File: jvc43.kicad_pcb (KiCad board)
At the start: 6 copper layers, 101.6 x 50.8 mm, 119 parts, among them J201 8P8C_LED_Shielded, J301 8P8C_LED_Shielded, J401 USB_C_Receptacle_USB2.0, U201 LAN8810, U301 LAN8810, U401 LTC3622*DE

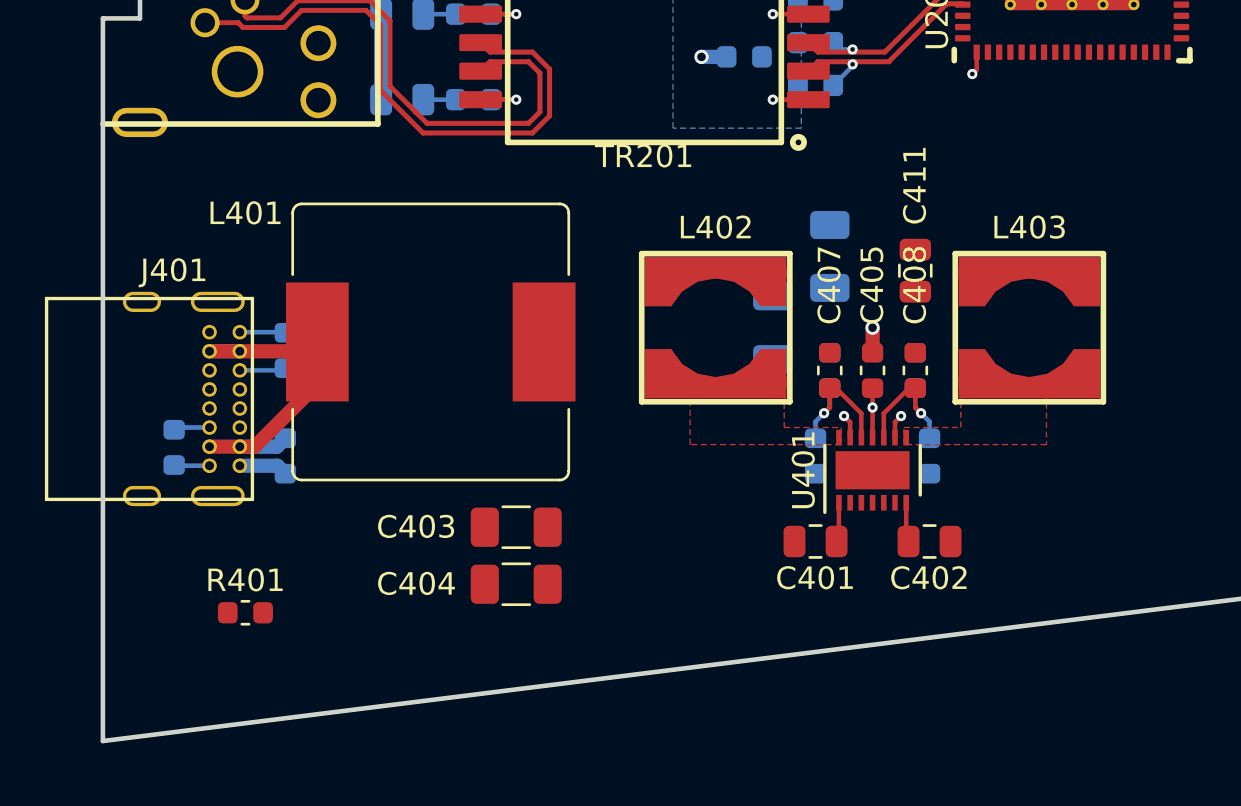
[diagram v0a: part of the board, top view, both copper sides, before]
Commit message: Major work on the power supply: - Swapped the input filter inductor for a significantly smaller one - Basically finished laying out the switching supply
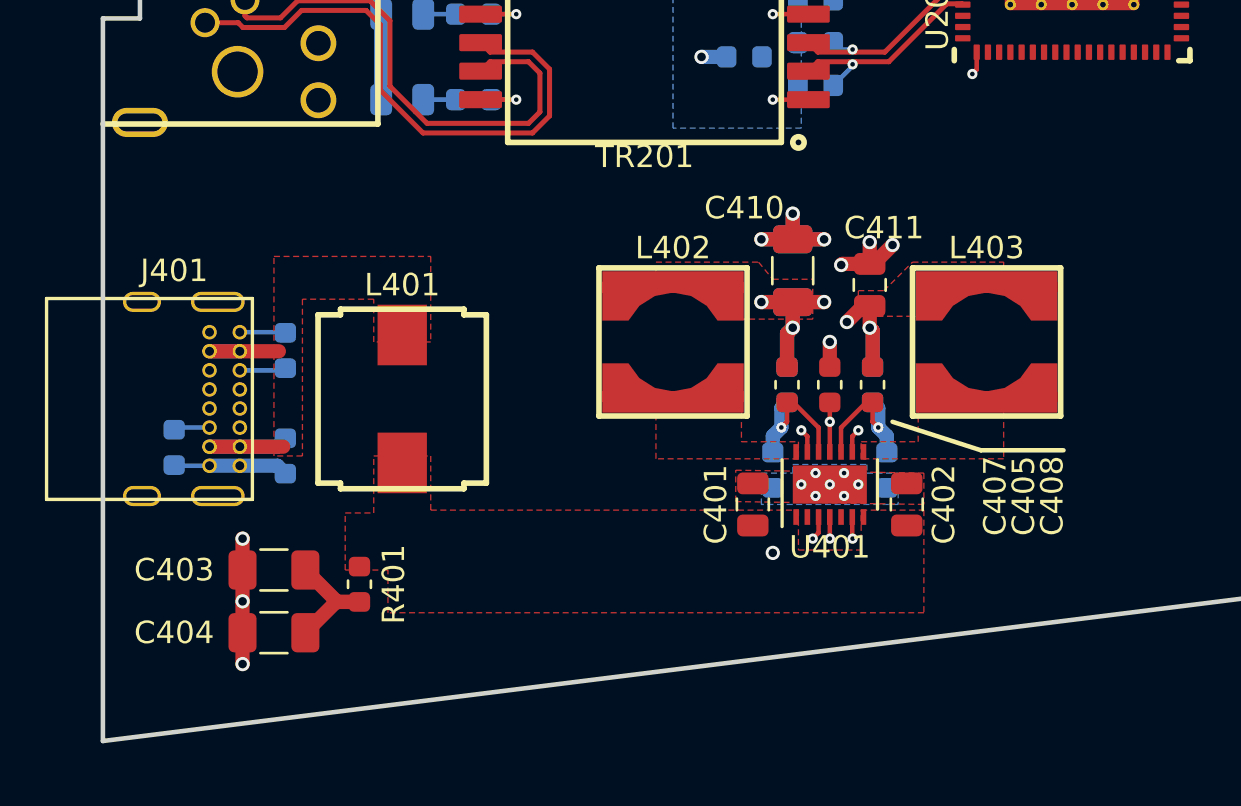
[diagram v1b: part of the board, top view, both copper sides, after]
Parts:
- C410: moved to F.Cu
- L401: footprint Inductor_SMD:L_Bourns_SRR1210A -> myfp:L_Panasonic_ETQ-P4MxxxKFM
- moved C404 11.0 mm to (33.0, 71.4), turned to 180 degrees
- moved C403 11.0 mm to (33.0, 68.6), turned to 180 degrees
- moved R401 5.24 mm to (36.8, 69.2), turned to 270 degrees
- moved C401 3.25 mm to (54.4, 65.7), turned to 90 degrees
- moved L401 2.84 mm to (38.7, 61.0), turned to 270 degrees
- moved C409 2.69 mm to (56.1, 55.2), turned to 90 degrees
- moved C411 2.13 mm to (59.6, 55.9)
- moved C405 2.01 mm to (57.8, 60.3)
- moved C408 2.01 mm to (59.7, 60.3)
- moved L402 2.01 mm to (50.8, 58.4)
- moved L403 2.01 mm to (64.8, 58.4)
- moved R405 2.01 mm to (59.7, 60.3)
- moved R406 2.01 mm to (55.2, 64.1)
- moved U401 2.01 mm to (57.8, 64.8)
- moved C407 2.01 mm to (55.9, 60.3)
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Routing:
- net GND: track 28.7 -> 49.2 mm, vias 14 -> 32
- net +1V2: track 0.00 -> 11.6 mm, vias 0 -> 3
- net /Power_Supply/IntVcc: track 2.21 -> 10.9 mm, vias 1 -> 2
- net /Power_Supply/Vin_damp: track 0.00 -> 5.98 mm
- net +2V5: track 0.00 -> 5.89 mm, vias 0 -> 2
- net /Power_Supply/VCC_USB: track 16.3 -> 11.3 mm
- net /Power_Supply/PS_Vin: track 5.68 -> 2.91 mm, vias 2 -> 3
- added copper zone on F.Cu, net +1V2
- added copper zone on F.Cu, net +2V5
- added copper zone on F.Cu, net /Power_Supply/PS_Vin
- added copper zone on L3.Cu, net /Power_Supply/PS_Vin
- added copper zone on F.Cu, net /Power_Supply/VCC_USB
- added copper zone on B.Cu, net GND
- added copper zone on F.Cu, net GND

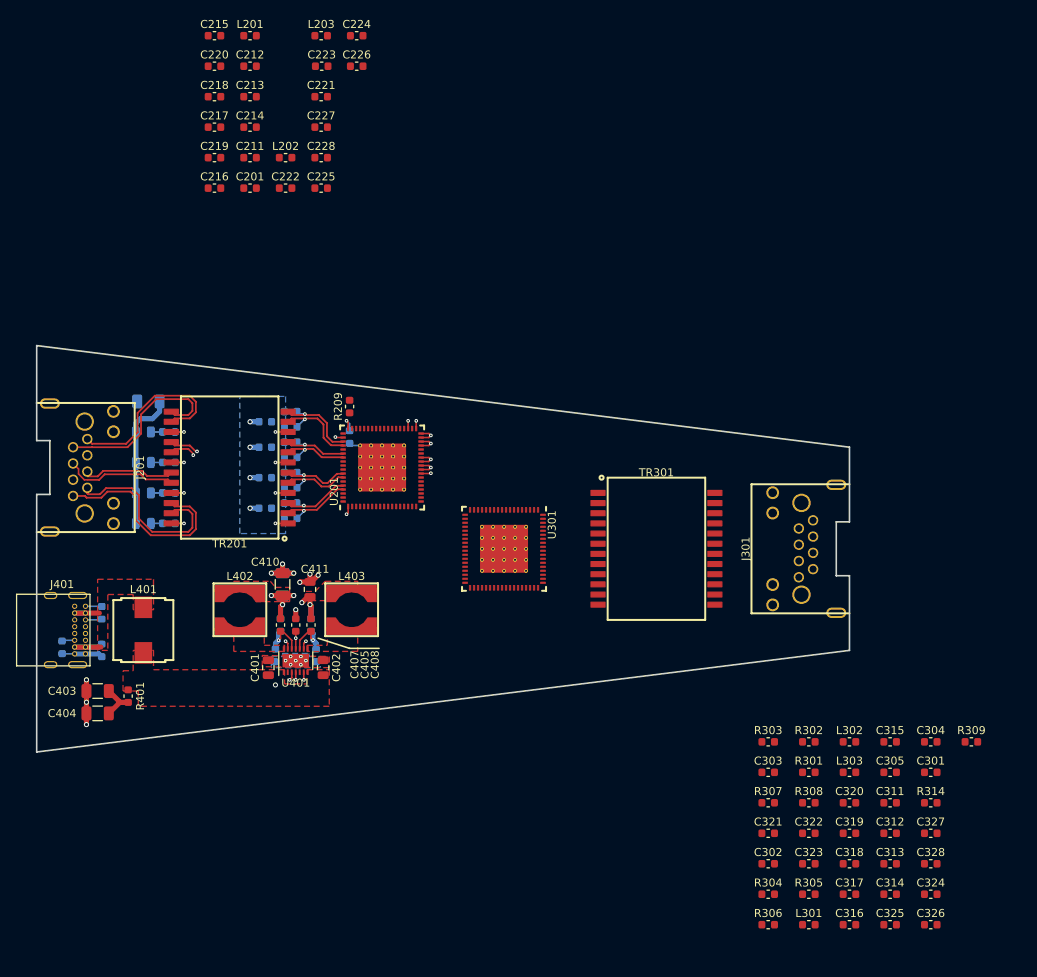
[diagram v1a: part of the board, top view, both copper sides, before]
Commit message: Forward progress - Started the real 1.2V power plane - Placed and routed most of PHY1 decoupling capacitors - Placed and partly routed transformer2 PHY-side resistors & capacitors - Labelled a few more nets for clarity during layout
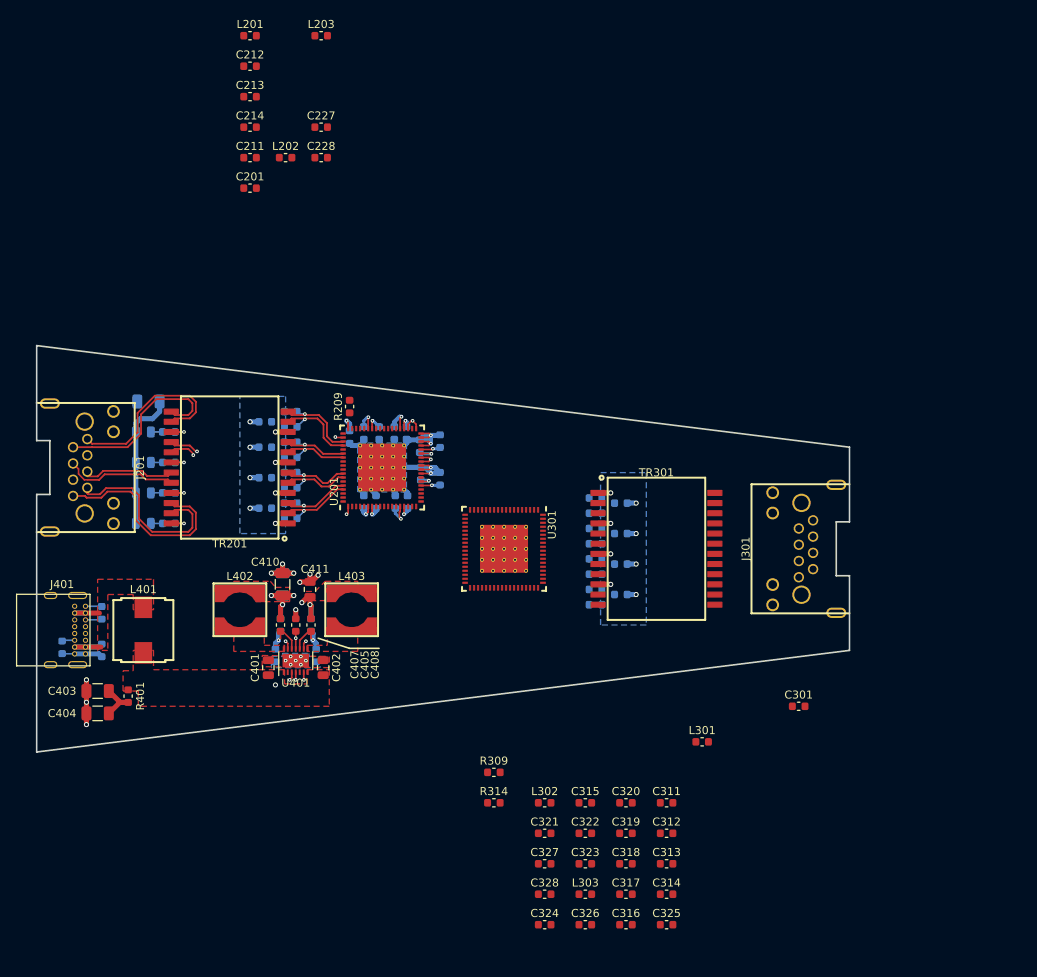
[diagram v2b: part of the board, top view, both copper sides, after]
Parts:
- C215, C216, C217, C218, C219, C220, C221, C222, C223, C224, C225, C226, C302, C303, C304, C305, R301, R302, R303, R304, R305, R306, R307, R308: moved to B.Cu
- moved C215 61.2 mm to (66.3, 45.0), turned to 90 degrees
- moved R309 59.8 mm to (82.5, 78.7)
- moved R314 54.6 mm to (82.5, 82.5)
- moved R306 54.0 mm to (95.2, 48.3), turned to 180 degrees
- moved C223 52.4 mm to (73.4, 41.4), turned to 90 degrees
- moved C217 52.2 mm to (75.8, 42.0), turned to 90 degrees
- moved C224 51.9 mm to (73.3, 38.0), turned to 90 degrees
- moved C218 51.5 mm to (75.8, 37.3), turned to 90 degrees
- moved R305 51.3 mm to (95.2, 50.2), turned to 180 degrees
- moved C221 51.1 mm to (67.8, 45.0), turned to 90 degrees
- moved C220 49.5 mm to (66.3, 36.3), turned to 270 degrees
- moved C324 48.4 mm to (88.9, 97.8)
- moved C327 48.4 mm to (88.9, 90.2)
- moved C328 48.4 mm to (88.9, 94.0)
- moved C305 47.6 mm to (98.4, 45.1)
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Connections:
- net Net-(U201-Pad20) renamed /Ethernet1/CRS
- net Net-(U201-Pad21) renamed /Ethernet1/COL
- net Net-(U201-Pad3) renamed /Ethernet1/TDO
- net Net-(U201-Pad42) renamed /Ethernet1/ACT_LED
- net Net-(U201-Pad43) renamed /Ethernet1/1000_LED
- net Net-(U201-Pad44) renamed /Ethernet1/100_LED
- net Net-(U201-Pad45) renamed /Ethernet1/10_LED
- net Net-(U201-Pad46) renamed /Ethernet1/CONFIG3
- net Net-(U201-Pad47) renamed /Ethernet1/CONFIG2
- net Net-(U201-Pad5) renamed /Ethernet1/XO
- net Net-(U201-Pad50) renamed /Ethernet1/CONFIG1
- net Net-(U201-Pad51) renamed /Ethernet1/CONFIG0
- net Net-(U201-Pad55) renamed /Ethernet1/nRST
- net Net-(U301-Pad20) renamed /Ethernet2/CRS
- net Net-(U301-Pad21) renamed /Ethernet2/COL
- net Net-(U301-Pad3) renamed /Ethernet2/TDO
- net Net-(U301-Pad42) renamed /Ethernet2/ACT_LED
- net Net-(U301-Pad43) renamed /Ethernet2/1000_LED
- net Net-(U301-Pad44) renamed /Ethernet2/100_LED
- net Net-(U301-Pad45) renamed /Ethernet2/10_LED
- net Net-(U301-Pad46) renamed /Ethernet2/CONFIG3
- net Net-(U301-Pad47) renamed /Ethernet2/CONFIG2
- net Net-(U301-Pad5) renamed /Ethernet2/XO
- net Net-(U301-Pad50) renamed /Ethernet2/CONFIG1
- net Net-(U301-Pad51) renamed /Ethernet2/CONFIG0
- net Net-(U301-Pad55) renamed /Ethernet2/nRST
- C215 pad 1: /Ethernet1/VDDVARIO -> +2V5
- C216 pad 1: /Ethernet1/VDDVARIO -> +2V5
- C217 pad 1: /Ethernet1/VDDVARIO -> +2V5
- C218 pad 1: /Ethernet1/VDDVARIO -> +2V5
- C219 pad 1: /Ethernet1/VDDVARIO -> +2V5
- C220 pad 1: /Ethernet1/VDDVARIO -> +2V5
- C315 pad 1: /Ethernet2/VDDVARIO -> +2V5
- C316 pad 1: /Ethernet2/VDDVARIO -> +2V5
- C317 pad 1: /Ethernet2/VDDVARIO -> +2V5
- C318 pad 1: /Ethernet2/VDDVARIO -> +2V5
- C319 pad 1: /Ethernet2/VDDVARIO -> +2V5
- C320 pad 1: /Ethernet2/VDDVARIO -> +2V5
- L201 pad 1: /Ethernet1/VDDVARIO -> +2V5
- L301 pad 1: /Ethernet2/VDDVARIO -> +2V5
- R209 pad 2: /Ethernet1/VDDVARIO -> +2V5
- R309 pad 2: /Ethernet2/VDDVARIO -> +2V5
- U201 pad 14: /Ethernet1/VDDVARIO -> +2V5
- U201 pad 2: /Ethernet1/VDDVARIO -> +2V5
- U201 pad 23: /Ethernet1/VDDVARIO -> +2V5
- U201 pad 32: /Ethernet1/VDDVARIO -> +2V5
- U201 pad 41: /Ethernet1/VDDVARIO -> +2V5
- U201 pad 49: /Ethernet1/VDDVARIO -> +2V5
- U201 pad 6: /Ethernet1/VDDVARIO -> +2V5
- U201 pad 72: /Ethernet1/VDDVARIO -> +2V5
- U301 pad 14: /Ethernet2/VDDVARIO -> +2V5
- U301 pad 2: /Ethernet2/VDDVARIO -> +2V5
- U301 pad 23: /Ethernet2/VDDVARIO -> +2V5
- U301 pad 32: /Ethernet2/VDDVARIO -> +2V5
- U301 pad 4: /Ethernet2/XI -> /Ethernet1/XI
- U301 pad 41: /Ethernet2/VDDVARIO -> +2V5
- U301 pad 49: /Ethernet2/VDDVARIO -> +2V5
- U301 pad 6: /Ethernet2/VDDVARIO -> +2V5
- U301 pad 72: /Ethernet2/VDDVARIO -> +2V5
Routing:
- net GND: track 49.2 -> 76.8 mm, vias 32 -> 35
- net +2V5: track 5.89 -> 22.2 mm, vias 2 -> 8
- net +1V2: track 11.6 -> 24.2 mm, vias 3 -> 9
- net /Ethernet2/VDD_ETH: track 0.00 -> 6.35 mm, vias 0 -> 4
- added copper zone on L3.Cu, net +1V2
- added copper zone on L5.Cu, net +2V5
- added copper zone on B.Cu, net /Ethernet2/VDD_ETH
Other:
- net class CloseSig added: clearance 0.1778, trace_width 0.2032, via_dia 0.4572, via_drill 0.2032

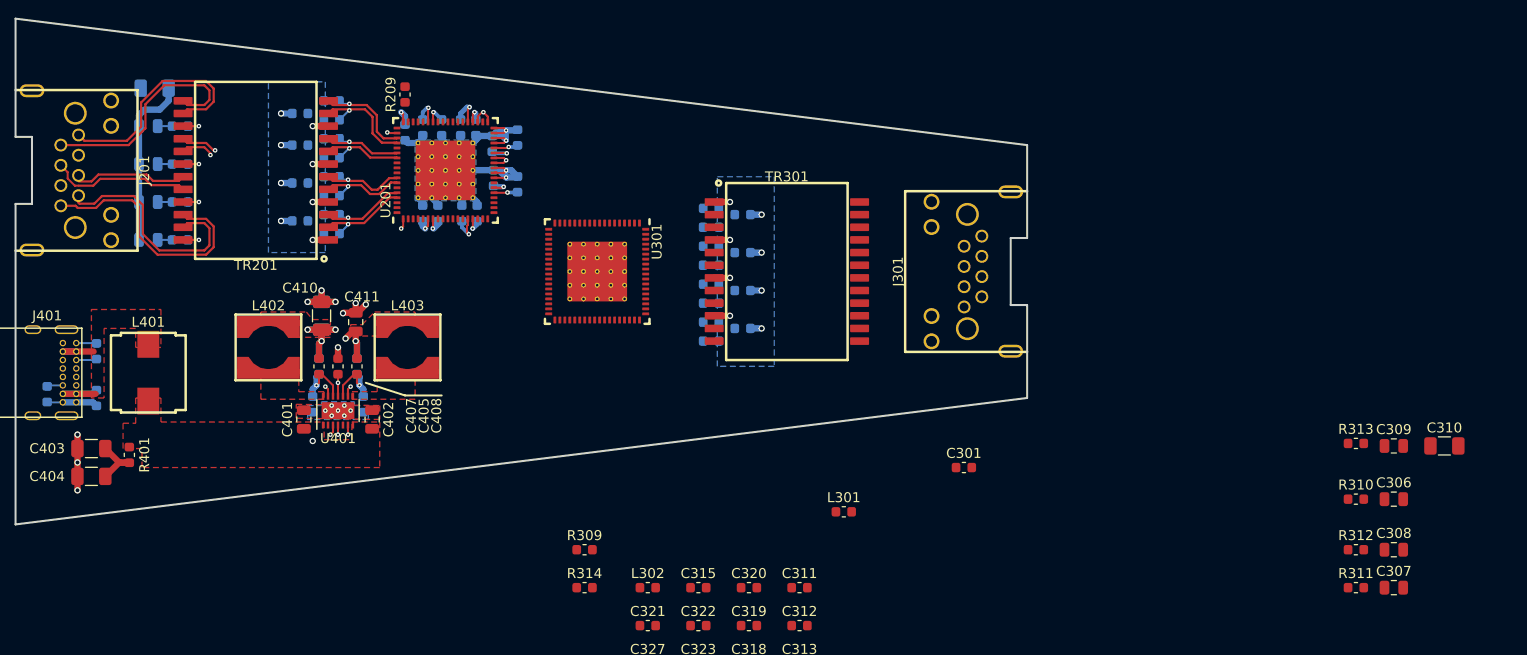
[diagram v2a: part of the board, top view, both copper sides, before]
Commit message: Routed Ethernet2 RJ45-to-transformer area.
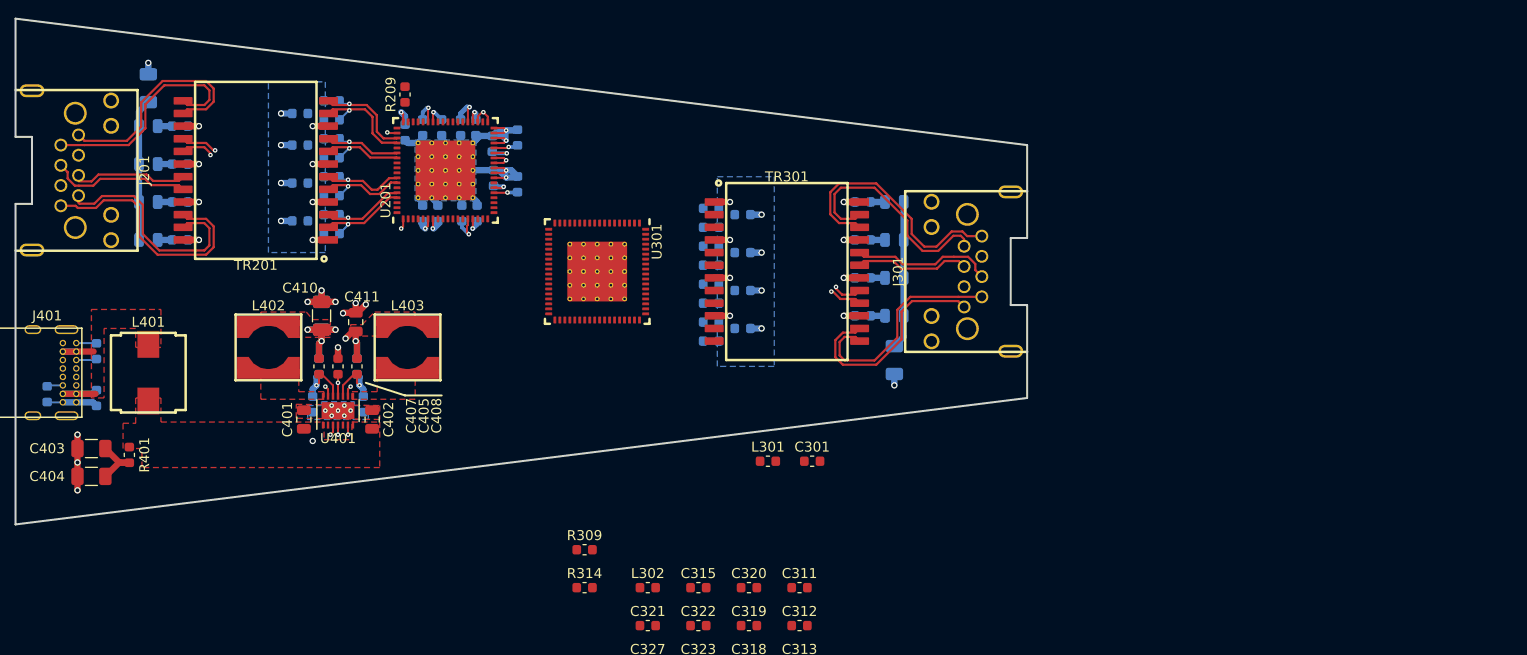
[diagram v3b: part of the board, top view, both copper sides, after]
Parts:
- C306, C307, C308, C309, C310, R310, R311, R312, R313: moved to B.Cu
- moved C307 59.0 mm to (113.7, 51.4)
- moved C308 59.0 mm to (113.7, 47.6)
- moved R311 58.5 mm to (110.5, 51.4)
- moved R312 58.5 mm to (110.5, 47.6)
- moved C310 55.9 mm to (113.7, 59.7), turned to 270 degrees
- moved C309 55.8 mm to (113.7, 43.8)
- moved R313 55.1 mm to (110.5, 43.8)
- moved C306 53.4 mm to (113.7, 55.2)
- moved R310 52.8 mm to (110.5, 55.2)
- moved C301 15.3 mm to (105.4, 69.8)
- moved L301 9.16 mm to (101.0, 69.8)
- moved C210 0.63 mm to (38.7, 32.4), turned to 90 degrees
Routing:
- net /Ethernet2/ETH_TX3-: track 0.00 -> 25.6 mm
- net /Ethernet2/ETH_TX1-: track 0.00 -> 23.6 mm, vias 0 -> 1
- net /Ethernet2/ETH_TX3+: track 0.00 -> 23.1 mm
- net /Ethernet2/ETH_TX0-: track 0.00 -> 22.5 mm
- net /Ethernet2/ETH_TX0+: track 0.00 -> 22.4 mm
- net /Ethernet2/ETH_TX1+: track 0.00 -> 19.4 mm, vias 0 -> 1
- net /Ethernet2/eth_inter_gnd: track 0.00 -> 14.9 mm
- net /Ethernet2/ETH_TX2+: track 0.00 -> 14.3 mm
- net /Ethernet2/ETH_TX2-: track 0.00 -> 11.5 mm
- net /Ethernet1/eth_inter_gnd: track 17.4 -> 14.2 mm
- net /Ethernet2/ETH_CT3: track 0.00 -> 2.71 mm, vias 0 -> 1
- net /Ethernet2/ETH_CT2: track 0.00 -> 2.71 mm, vias 0 -> 1
- net /Ethernet2/ETH_CT1: track 0.00 -> 2.71 mm, vias 0 -> 1
- net /Ethernet2/ETH_CT0: track 0.00 -> 2.71 mm, vias 0 -> 1
- net Net-(C309-Pad1): track 0.00 -> 1.45 mm
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- added copper zone on L2.Cu, net /Ethernet2/gnd_eth
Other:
- net class Diff100 added: clearance 0.20574, trace_width 0.22352, via_dia 0.4572, via_drill 0.2032
